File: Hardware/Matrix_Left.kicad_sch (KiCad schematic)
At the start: 130 parts, among them SW10 PG1350, SW11 PG1350, SW12 PG1350, SW13 PG1350, SW14 PG1350, SW15 PG1350, SW16 PG1350, SW17 PG1350, SW18 PG1350, SW19 PG1350, SW20 PG1350, SW21 PG1350, SW22 PG1350, SW23 PG1350, SW24 PG1350, SW25 PG1350, SW26 PG1350, SW27 PG1350, SW28 PG1350, SW29 PG1350, SW3 PG1350, SW30 PG1350, SW31 PG1350, SW32 ENCODER, SW4 PG1350, SW5 PG1350, SW6 PG1350, SW7 PG1350, SW8 PG1350, SW9 PG1350

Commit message: Layout coordination
Coordinated the layout with the schematic.
Finished the initial switch layout.
Need to decide on a complete layout for the keyboard and assign the auxiliary keys.
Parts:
- removed C17, C22, C27, C32, C37: 1u, Capacitor_SMD:C_0603_1608Metric, symbol Device:C
- removed D11, D21, D31, D41, D51: SK6812MINI-E, Custom_Parts:LED_SK6812MINI-E_3.2x2.8mm_P1.5mm_ReverseMount, symbol LED:SK6812MINI-E
- added C13: 1u, Capacitor_SMD:C_0603_1608Metric, symbol Device:C
- added D7: SK6812MINI-E, Custom_Parts:LED_SK6812MINI-E_3.2x2.8mm_P1.5mm_ReverseMount, symbol LED:SK6812MINI-E
- renumbered C13 to C14, C14 to C15, C15 to C16, C16 to C17, C23 to C22, C24 to C23, C25 to C24, C26 to C25, C28 to C26, C29 to C27, C30 to C28, C31 to C29, C33 to C30, C34 to C31, C35 to C32, C36 to C33, C38 to C34, C39 to C35, C40 to C36, C41 to C37, C42 to C38, C43 to C39, C44 to C40, C45 to C41, C46 to C42, C47 to C43, D9 to D10, D10 to D11, D14 to D12, D15 to D13, D16 to D14, D17 to D15, D18 to D16, D12 to D17, D13 to D18, D24 to D21, D25 to D22, D26 to D23, D27 to D24, D28 to D25, D22 to D26, D23 to D27, D29 to D28, D30 to D29, D34 to D30, D35 to D31, D36 to D32, D37 to D33, D38 to D34, D32 to D35, D33 to D36, D39 to D37, D40 to D38, D44 to D39, D45 to D40, D46 to D41, D47 to D42, D48 to D43, D42 to D44, D43 to D45, D49 to D46, D50 to D47, D52 to D48, D53 to D49, D54 to D50, D55 to D51, D56 to D52, D57 to D53, D58 to D54, D61 to D55, D62 to D56, D63 to D57, D64 to D58, D65 to D59, D59 to D60, D60 to D61, D66 to D62, D67 to D63, D68 to D64, D69 to D65, D7 to D8, D8 to D9
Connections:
- net 5VL: now also C13.1, D7.3 (VDD)
- net GND: now also C13.2, D7.1 (VSS)
- net LED_DATA_L: now also D7.2 (DIN); no longer D10.2 (DIN)
- new net: D10.2 (DIN), D7.4 (DOUT)
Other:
- moved on the sheet: C14, C15, C16, C17, C18, C19, C20, C21, C22, C23, C24, C25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

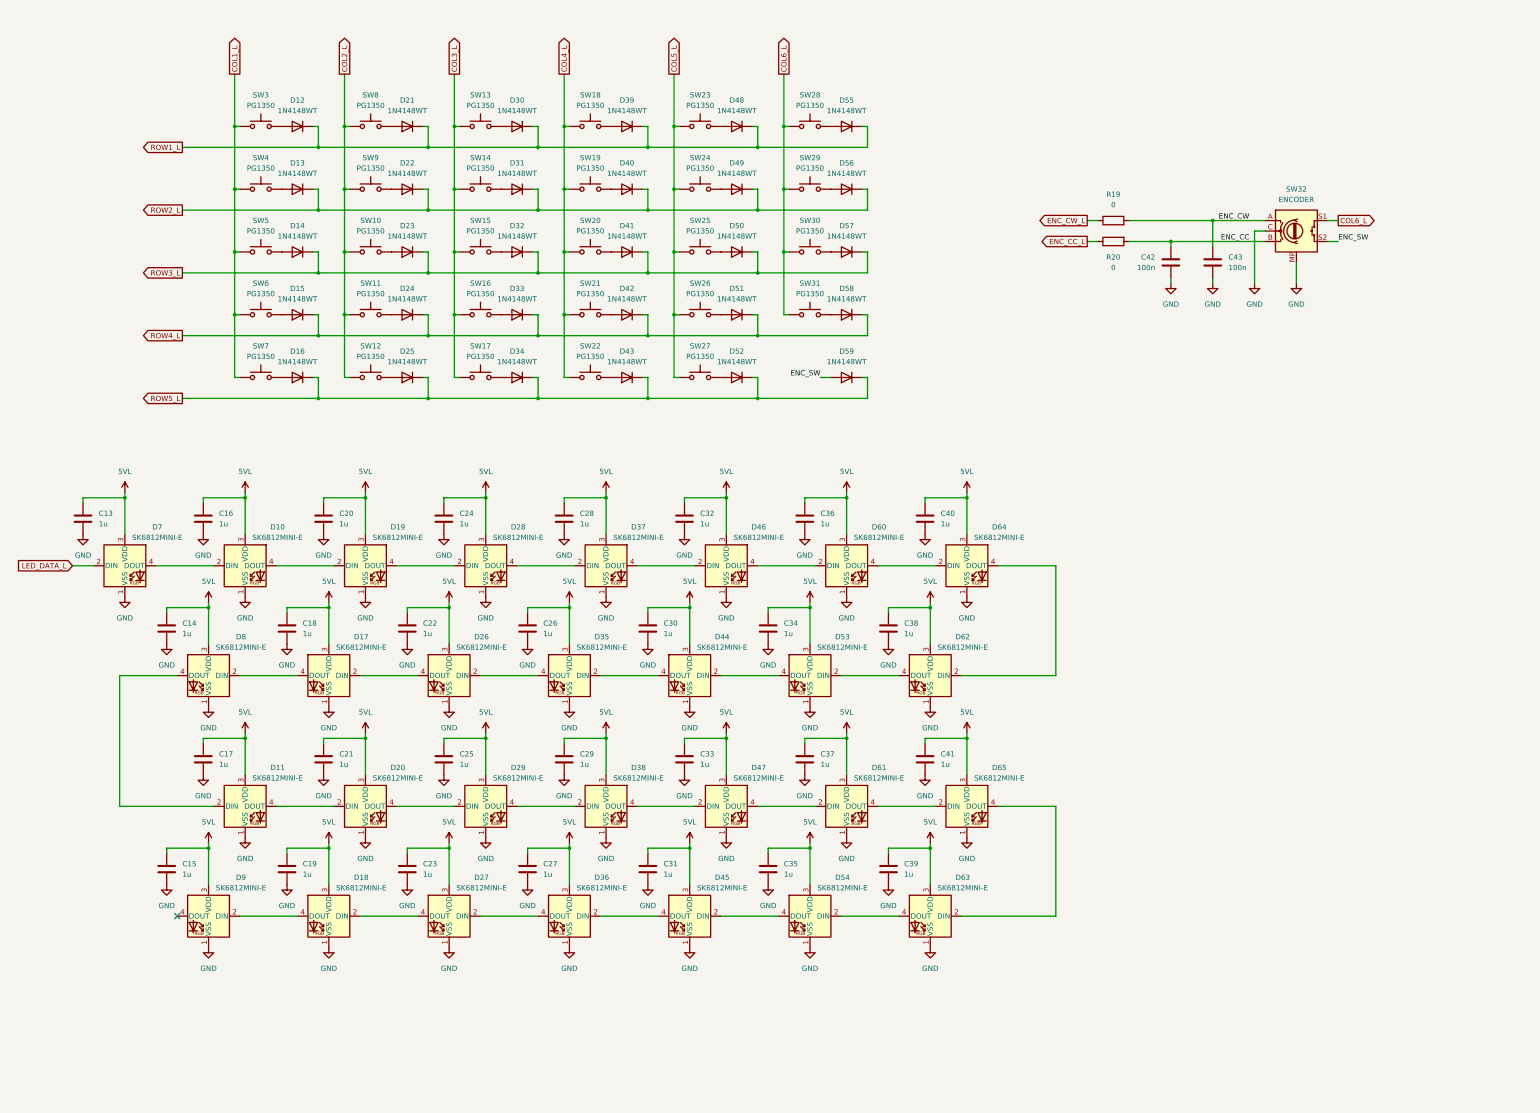
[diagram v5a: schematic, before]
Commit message: Key matrix and edges
Defined the key matrix locations and the board edges.
Next step: start routing and verify the buck converter layout.
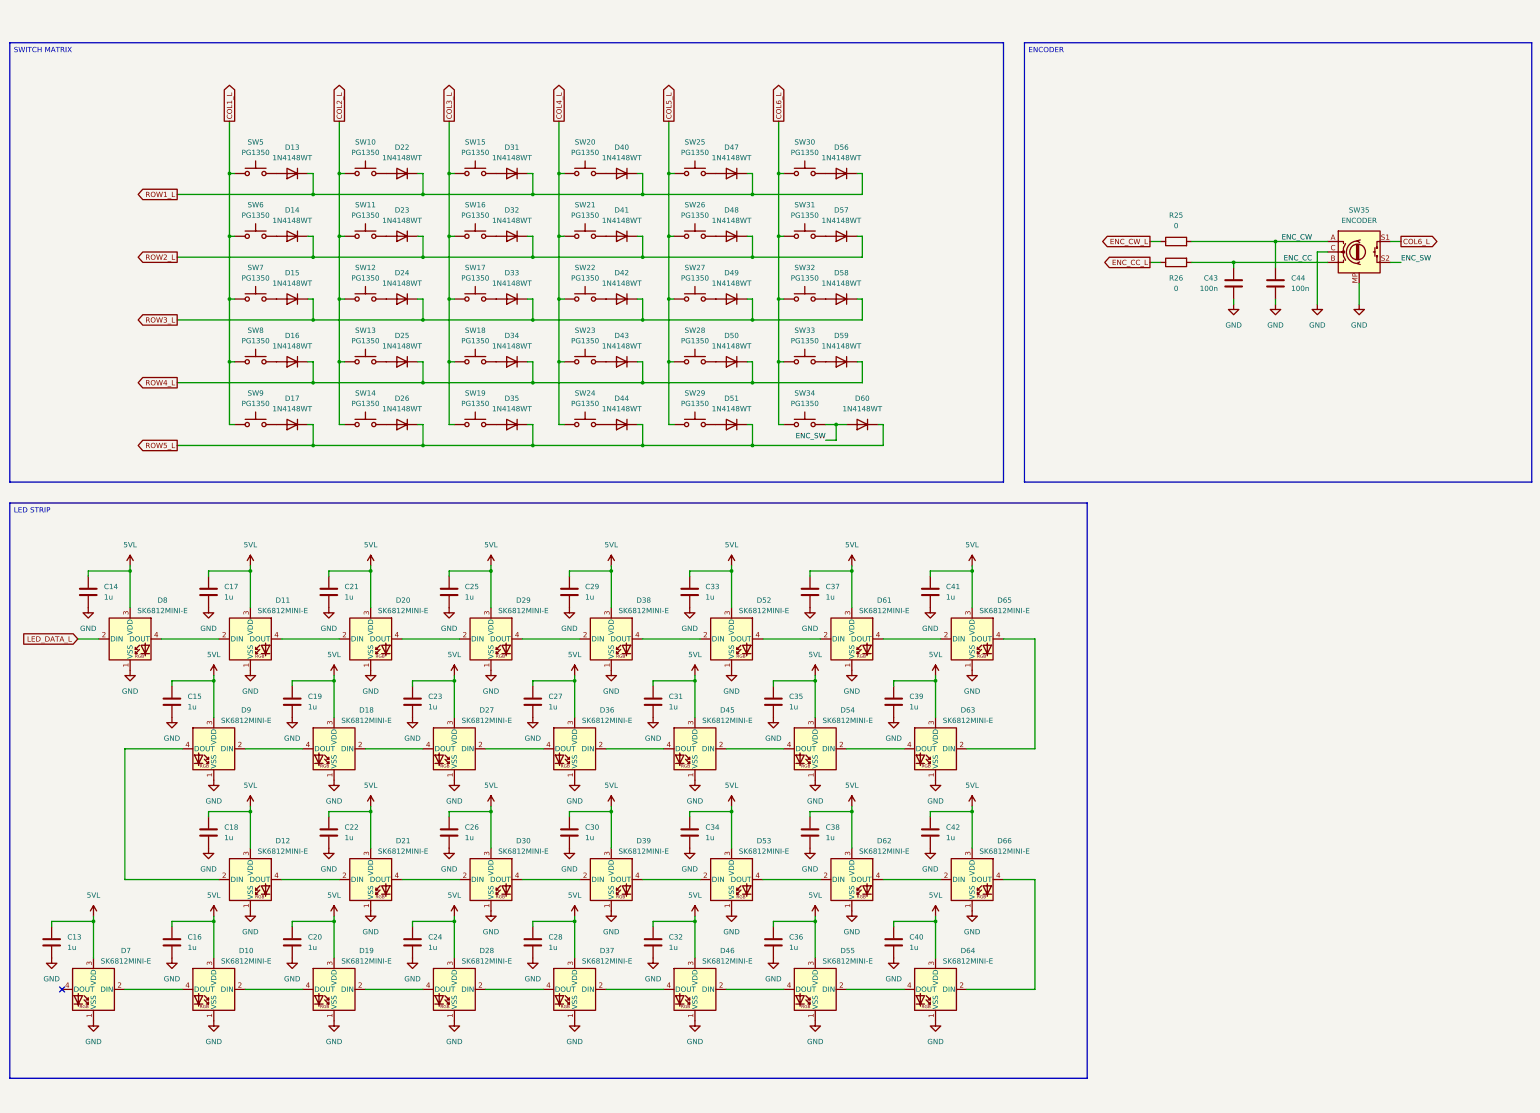
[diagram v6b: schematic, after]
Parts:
- removed C38: 1u, Capacitor_SMD:C_0603_1608Metric, symbol Device:C
- removed D55: 1N4148WT, Diode_SMD:D_SOD-523, symbol Diode:1N4148WT
- removed D62: SK6812MINI-E, Custom_Parts:LED_SK6812MINI-E_3.2x2.8mm_P1.5mm_ReverseMount, symbol LED:SK6812MINI-E
- removed SW27, SW28: PG1350, Custom_Parts:PG1350_1.00u_PCB, symbol Switch:SW_Push
- added C14, C42: 1u, Capacitor_SMD:C_0603_1608Metric, symbol Device:C
- added D60: 1N4148WT, Diode_SMD:D_SOD-523, symbol Diode:1N4148WT
- added D66, D8: SK6812MINI-E, Custom_Parts:LED_SK6812MINI-E_3.2x2.8mm_P1.5mm_ReverseMount, symbol LED:SK6812MINI-E
- added SW32, SW33, SW34: PG1350, Custom_Parts:PG1350_1.00u_PCB, symbol Switch:SW_Push
- renumbered C14 to C15, C15 to C16, C16 to C17, C17 to C18, C18 to C19, C19 to C20, C20 to C21, C21 to C22, C22 to C23, C23 to C24, C24 to C25, C25 to C26, C26 to C27, C27 to C28, C28 to C29, C29 to C30, C30 to C31, C31 to C32, C32 to C33, C33 to C34, C34 to C35, C35 to C36, C36 to C37, C37 to C38, C42 to C43, C43 to C44, D9 to D10, D10 to D11, D11 to D12, D12 to D13, D13 to D14, D14 to D15, D15 to D16, D16 to D17, D17 to D18, D18 to D19, D19 to D20, D20 to D21, D21 to D22, D22 to D23, D23 to D24, D24 to D25, D25 to D26, D26 to D27, D27 to D28, D28 to D29, D29 to D30, D30 to D31, D31 to D32, D32 to D33, D33 to D34, D34 to D35, D35 to D36, D36 to D37, D37 to D38, D38 to D39, D39 to D40, D40 to D41, D41 to D42, D42 to D43, D43 to D44, D44 to D45, D45 to D46, D48 to D47, D49 to D48, D50 to D49, D51 to D50, D52 to D51, D46 to D52, D47 to D53, D53 to D54, D54 to D55, D60 to D61, D61 to D62, D8 to D9, R19 to R25, R20 to R26, SW8 to SW10, SW9 to SW11, SW10 to SW12, SW11 to SW13, SW12 to SW14, SW13 to SW15, SW14 to SW16, SW15 to SW17, SW16 to SW18, SW17 to SW19, SW18 to SW20, SW19 to SW21, SW20 to SW22, SW21 to SW23, SW22 to SW24, SW23 to SW25, SW24 to SW26, SW25 to SW27, SW26 to SW28, SW32 to SW35, SW3 to SW5, SW4 to SW6, SW5 to SW7, SW6 to SW8, SW7 to SW9
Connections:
- net 5VL: now also C14.1, C42.1, D66.3 (VDD), D8.3 (VDD)
- net COL5_L: now also SW29.1
- net COL6_L: now also SW32.1, SW33.1, SW34.1; no longer SW29.1
- net ENC_SW: now also D60.2 (A), SW34.2; no longer D59.2 (A)
- net GND: now also C14.2, C42.2, D66.1 (VSS), D8.1 (VSS)
- net LED_DATA_L: now also D8.2 (DIN); no longer D7.2 (DIN)
- net ROW1_L: now also D56.1 (K)
- net ROW2_L: now also D57.1 (K); no longer D56.1 (K)
- net ROW3_L: now also D58.1 (K); no longer D57.1 (K)
- net ROW4_L: now also D59.1 (K); no longer D58.1 (K)
- net ROW5_L: now also D60.1 (K); no longer D59.1 (K)
- net at D61.4 (DOUT): now also D65.2 (DIN); no longer D64.2 (DIN)
- net at SW30.2: now also D56.2 (A); no longer D57.2 (A)
- net at D64.4 (DOUT): now also D55.2 (DIN)
- net at D54.2 (DIN): now also D63.4 (DOUT)
- net at D62.4 (DOUT): now also D66.2 (DIN); no longer D65.2 (DIN)
- net at D58.2 (A): now also SW32.2; no longer SW31.2
- net at D10.4 (DOUT): now also D7.2 (DIN)
- net at SW29.2: now also D51.2 (A); no longer D56.2 (A)
- net at D7.4 (DOUT): no longer D11.2 (DIN)
- new net: D59.2 (A), SW33.2
- new net: D64.2 (DIN), D66.4 (DOUT)
- new net: D11.2 (DIN), D8.4 (DOUT)
- new net: D57.2 (A), SW31.2
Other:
- moved on the sheet: C15, C16, C17, C18, C19, C20, C21, C22, C23, C24, C25, C26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

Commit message: Pinout and footprints
Updated the MCU footprints because the silkscreen was too close to the edge.
Updated the pinout for the MCUs. The left side seems to be ok, but the right side may need some adjustments.
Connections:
- net COL6_L: no longer SW35.S1
- net GND: now also SW35.S2
- net ENC_SW: no longer names the net of D60.2 (A), SW34.2
- net ENC_SW: no longer SW35.S2
- new net ENC_SW_R: SW35.S1
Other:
- moved on the sheet: D60
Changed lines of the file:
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@@
 		)
 	)
-	(text_box "ENCODER"
+	(text_box "ROTARY ENCODER"
 		(exclude_from_sim no)
 		(at 273.05 22.86 0)
@@
 	)
 	(junction
-		(at 227.33 115.57)
-		(diameter 0)
-		(color 0 0 0 0)
-	)
-	(junction
 		(at 323.85 76.2)
 		(diameter 0)
@@
 	(wire
 		(pts
+			(xy 361.95 71.12) (xy 364.49 71.12)
+		)
+		(stroke
+			(width 0)
+			(type default)
+		)
+	)
+	(wire
+		(pts
 			(xy 99.06 69.85) (xy 100.33 69.85)
 		)
@@
 	(wire
 		(pts
-			(xy 238.76 115.57) (xy 238.76 120.65)
+			(xy 233.68 115.57) (xy 233.68 120.65)
 		)
 		(stroke
@@
 	(wire
 		(pts
-			(xy 227.33 115.57) (xy 224.79 115.57)
-		)
-		(stroke
-			(width 0)
-			(type default)
-		)
-	)
-	(wire
-		(pts
 			(xy 205.74 54.61) (xy 207.01 54.61)
 		)
@@
 	(wire
 		(pts
-			(xy 361.95 71.12) (xy 364.49 71.12)
-		)
-		(stroke
-			(width 0)
-			(type default)
-		)
-	)
-	(wire
-		(pts
 			(xy 133.35 100.33) (xy 134.62 100.33)
 		)
@@
 	(wire
 		(pts
+			(xy 361.95 76.2) (xy 364.49 76.2)
+		)
+		(stroke
+			(width 0)
+			(type default)
+		)
+	)
+	(wire
+		(pts
 			(xy 163.83 234.95) (xy 163.83 236.22)
 		)
@@
 	(wire
 		(pts
-			(xy 207.01 120.65) (xy 238.76 120.65)
+			(xy 207.01 120.65) (xy 233.68 120.65)
 		)
 		(stroke
@@
 	(wire
 		(pts
-			(xy 224.79 119.38) (xy 227.33 119.38)
-		)
-		(stroke
-			(width 0)
-			(type default)
-		)
-	)
-	(wire
-		(pts
-			(xy 229.87 115.57) (xy 227.33 115.57)
-		)
-		(stroke
-			(width 0)
-			(type default)
-		)
-	)
-	(wire
-		(pts
 			(xy 250.19 151.13) (xy 260.35 151.13)
 		)
@@
 	(wire
 		(pts
+			(xy 364.49 76.2) (xy 364.49 86.36)
+		)
+		(stroke
+			(width 0)
+			(type default)
+		)
+	)
+	(wire
+		(pts
 			(xy 83.82 252.73) (xy 97.79 252.73)
 		)
@@
 	(wire
 		(pts
-			(xy 237.49 115.57) (xy 238.76 115.57)
+			(xy 232.41 115.57) (xy 233.68 115.57)
 		)
 		(stroke
@@
 	(wire
 		(pts
-			(xy 361.95 76.2) (xy 364.49 76.2)
-		)
-		(stroke
-			(width 0)
-			(type default)
-		)
-	)
-	(wire
-		(pts
 			(xy 80.01 85.09) (xy 80.01 100.33)
 		)
@@
 	(wire
 		(pts
-			(xy 227.33 119.38) (xy 227.33 115.57)
-		)
-		(stroke
-			(width 0)
-			(type default)
-		)
-	)
-	(wire
-		(pts
 			(xy 193.04 236.22) (xy 193.04 245.11)
 		)
@@
 		)
 	)
-	(label "ENC_SW"
-		(at 364.49 76.2 0)
-		(effects
-			(font
-				(size 1.27 1.27)
-			)
-			(justify left bottom)
-		)
-	)
-	(label "ENC_SW"
-		(at 224.79 119.38 180)
-		(effects
-			(font
-				(size 1.27 1.27)
-			)
-			(justify right bottom)
-		)
-	)
 	(label "ENC_CC"
 		(at 342.9 76.2 180)
@@
 		)
 	)
-	(global_label "ROW3_L"
+	(global_label "ENC_SW_R"
 		(shape output)
-		(at 67.31 90.17 180)
+		(at 364.49 71.12 0)
 		(fields_autoplaced yes)
 		(effects
@@
 				(size 1.27 1.27)
 			)
-			(justify right)
+			(justify left)
 		)
 		(property "Intersheetrefs" "${INTERSHEET_REFS}"
-			(at 56.1001 90.17 0)
+			(at 377.0908 71.12 0)
 			(hide yes)
 			(show_name no)
@@
 					(size 1.27 1.27)
 				)
-				(justify right)
+				(justify left)
 			)
 		)
 	)
-	(global_label "COL4_L"
+	(global_label "ROW3_L"
 		(shape output)
-		(at 160.02 41.91 90)
+		(at 67.31 90.17 180)
 		(fields_autoplaced yes)
 		(effects
@@
 				(size 1.27 1.27)
 			)
-			(justify left)
+			(justify right)
 		)
 		(property "Intersheetrefs" "${INTERSHEET_REFS}"
-			(at 160.02 31.1234 90)
+			(at 56.1001 90.17 0)
 			(hide yes)
 			(show_name no)
@@
 					(size 1.27 1.27)
 				)
-				(justify left)
+				(justify right)
 			)
 		)
 	)
-	(global_label "ROW4_L"
+	(global_label "COL4_L"
 		(shape output)
-		(at 67.31 105.41 180)
+		(at 160.02 41.91 90)
 		(fields_autoplaced yes)
 		(effects
@@
 				(size 1.27 1.27)
 			)
-			(justify right)
+			(justify left)
 		)
 		(property "Intersheetrefs" "${INTERSHEET_REFS}"
-			(at 56.1001 105.41 0)
+			(at 160.02 31.1234 90)
 			(hide yes)
 			(show_name no)
@@
 					(size 1.27 1.27)
 				)
-				(justify right)
+				(justify left)
 			)
 		)
 	)
-	(global_label "COL6_L"
+	(global_label "ROW4_L"
 		(shape output)
-		(at 364.49 71.12 0)
+		(at 67.31 105.41 180)
 		(fields_autoplaced yes)
 		(effects
@@
 				(size 1.27 1.27)
 			)
-			(justify left)
+			(justify right)
 		)
 		(property "Intersheetrefs" "${INTERSHEET_REFS}"
-			(at 374.309 71.12 0)
+			(at 56.1001 105.41 0)
 			(hide yes)
 			(show_name no)
@@
 					(size 1.27 1.27)
 				)
-				(justify left)
+				(justify right)
 			)
 		)
@@
 	)
 	(symbol
+		(lib_id "power:GND")
+		(at 364.49 86.36 0)
+		(unit 1)
+		(body_style 1)
+		(exclude_from_sim no)
+		(in_bom yes)
+		(on_board yes)
+		(in_pos_files yes)
+		(dnp no)
+		(fields_autoplaced yes)
+		(property "Reference" "#PWR0254"
+			(at 364.49 92.71 0)
+			(hide yes)
+			(show_name no)
+			(do_not_autoplace no)
+			(effects
+				(font
+					(size 1.27 1.27)
+				)
+			)
+		)
+		(property "Value" "GND"
+			(at 364.49 91.44 0)
+			(show_name no)
+			(do_not_autoplace no)
+			(effects
+				(font
+					(size 1.27 1.27)
+				)
+			)
+		)
+		(property "Footprint" ""
+			(at 364.49 86.36 0)
+			(hide yes)
+			(show_name no)
+			(do_not_autoplace no)
+			(effects
+				(font
+					(size 1.27 1.27)
+				)
+			)
+		)
+		(property "Datasheet" ""
+			(at 364.49 86.36 0)
+			(hide yes)
+			(show_name no)
+			(do_not_autoplace no)
+			(effects
+				(font
+					(size 1.27 1.27)
+				)
+			)
+		)
+		(property "Description" "Power symbol creates a global label with name \"GND\" , ground"
+			(at 364.49 86.36 0)
+			(hide yes)
+			(show_name no)
+			(do_not_autoplace no)
+			(effects
+				(font
+					(size 1.27 1.27)
+				)
+			)
+		)
+		(pin "1"
+		)
+		(instances
+			(project "ValkiriaSplit"
+				(path "/7a2b6783-81dc-46bd-bbde-89342e0b1c5b/e947cf9a-ba73-4488-995e-2b26770a6850"
+					(reference "#PWR0254")
+					(unit 1)
+				)
+			)
+		)
+	)
+	(symbol
 		(lib_id "Device:C")
 		(at 191.77 156.21 0)
@@
 	(symbol
 		(lib_id "Diode:1N4148WT")
-		(at 233.68 115.57 180)
+		(at 228.6 115.57 180)
 		(unit 1)
 		(body_style 1)
@@
 		(fields_autoplaced yes)
 		(property "Reference" "D60"
-			(at 233.68 109.22 0)
+			(at 228.6 109.22 0)
 			(show_name no)
 			(do_not_autoplace no)
@@
 		)
 		(property "Value" "1N4148WT"
-			(at 233.68 111.76 0)
+			(at 228.6 111.76 0)
 			(show_name no)
 			(do_not_autoplace no)
@@
 		)
 		(property "Footprint" "Diode_SMD:D_SOD-523"
-			(at 233.68 111.125 0)
+			(at 228.6 111.125 0)
 			(hide yes)
 			(show_name no)
@@
 		)
 		(property "Datasheet" "https://www.diodes.com/assets/Datasheets/ds30396.pdf"
-			(at 233.68 115.57 0)
+			(at 228.6 115.57 0)
 			(hide yes)
 			(show_name no)
@@
 		)
 		(property "Description" "75V 0.15A Fast switching Diode, SOD-523"
-			(at 233.68 115.57 0)
+			(at 228.6 115.57 0)
 			(hide yes)
 			(show_name no)
@@
 		)
 		(property "Sim.Device" "D"
-			(at 233.68 115.57 0)
+			(at 228.6 115.57 0)
 			(hide yes)
 			(show_name no)
@@
 		)
 		(property "Sim.Pins" "1=K 2=A"
-			(at 233.68 115.57 0)
+			(at 228.6 115.57 0)
 			(hide yes)
 			(show_name no)
@@
 		)
 		(property "JLC Part" "C7420320"
-			(at 233.68 115.57 0)
+			(at 228.6 115.57 0)
 			(hide yes)
 			(show_name no)
@@
 		)
 		(property "Manufacturer Part" "1N4148WT"
-			(at 233.68 115.57 0)
+			(at 228.6 115.57 0)
 			(hide yes)
 			(show_name no)

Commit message: Reset button and LED switch
Added an LED power switch.
Returned the reset button for bootloader access.
Focus on changing the display to an e-ink one for lower power consumption.
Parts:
- renumbered R25 to R23, R26 to R24, SW8 to SW10, SW9 to SW11, SW10 to SW12, SW11 to SW13, SW12 to SW14, SW13 to SW15, SW14 to SW16, SW15 to SW17, SW16 to SW18, SW17 to SW19, SW18 to SW20, SW19 to SW21, SW20 to SW22, SW21 to SW23, SW22 to SW24, SW23 to SW25, SW24 to SW26, SW25 to SW27, SW26 to SW28, SW27 to SW29, SW28 to SW30, SW29 to SW31, SW30 to SW32, SW31 to SW33, SW32 to SW34, SW33 to SW35, SW34 to SW36, SW35 to SW37, SW5 to SW7, SW6 to SW8, SW7 to SW9
